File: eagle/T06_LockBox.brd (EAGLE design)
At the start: 100 x 80 mm, 28 parts, among them T1 2N3904, T2 2N3904, T3 2N3904

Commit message: small changes
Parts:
- moved R7 92.9 mm to (55.4, 8.38), turned to 180 degrees
- moved R6 92.1 mm to (55.4, 10.7), turned to 180 degrees
- moved R10 88.3 mm to (38.6, 10.7), turned to 90 degrees
- moved R3 85.8 mm to (47.2, 20.6)
- moved T3 83.8 mm to (53.3, 20.8)
- moved R9 83.0 mm to (35.3, 10.4), turned to 90 degrees
- moved R2 83.0 mm to (47.5, 18.2), turned to 180 degrees
- moved R4 81.6 mm to (84.3, 2.79)
- moved D1 79.2 mm to (91.4, 15.5), turned to 270 degrees
- moved R8 78.4 mm to (32.5, 10.7), turned to 90 degrees
- moved U$2 75.7 mm to (84.5, 58.4)
- moved JP1 75.3 mm to (90.3, 2.79)
- moved T2 74.1 mm to (53.5, 15.0)
- moved C5 67.9 mm to (89.3, 68.7), turned to 180 degrees
- moved R5 67.0 mm to (21.3, 20.3)
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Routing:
- net A0: track 69.3 -> 0.00 mm
- net A1: track 66.0 -> 0.00 mm
- net A2: track 55.2 -> 0.00 mm
- net START: track 20.0 -> 0.00 mm
- net 3.3V: track 3.52 -> 0.00 mm

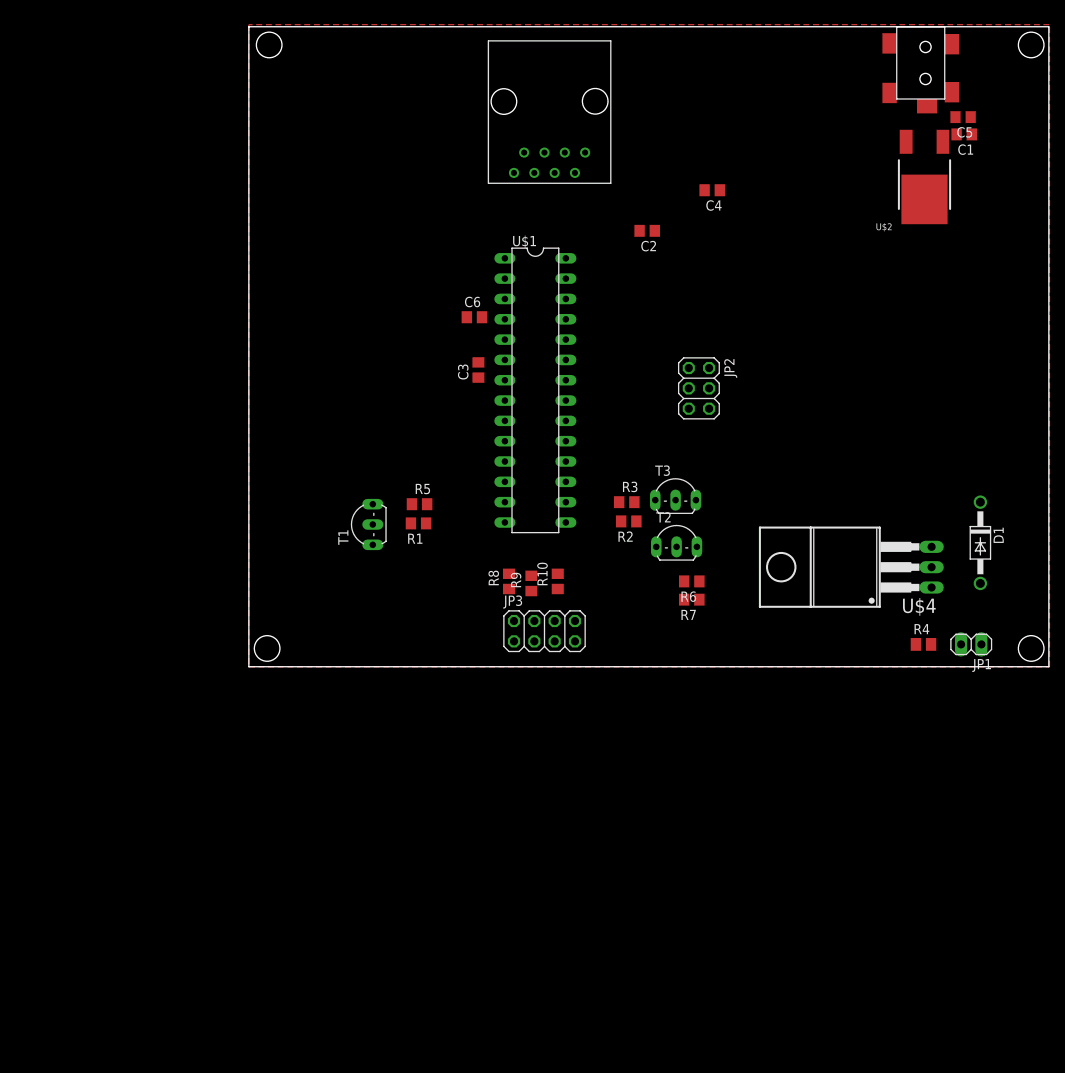
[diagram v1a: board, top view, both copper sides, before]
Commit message: Added connections to unused pins on the schematic.  Finished routing wires to the unused pin header locaton on the board.
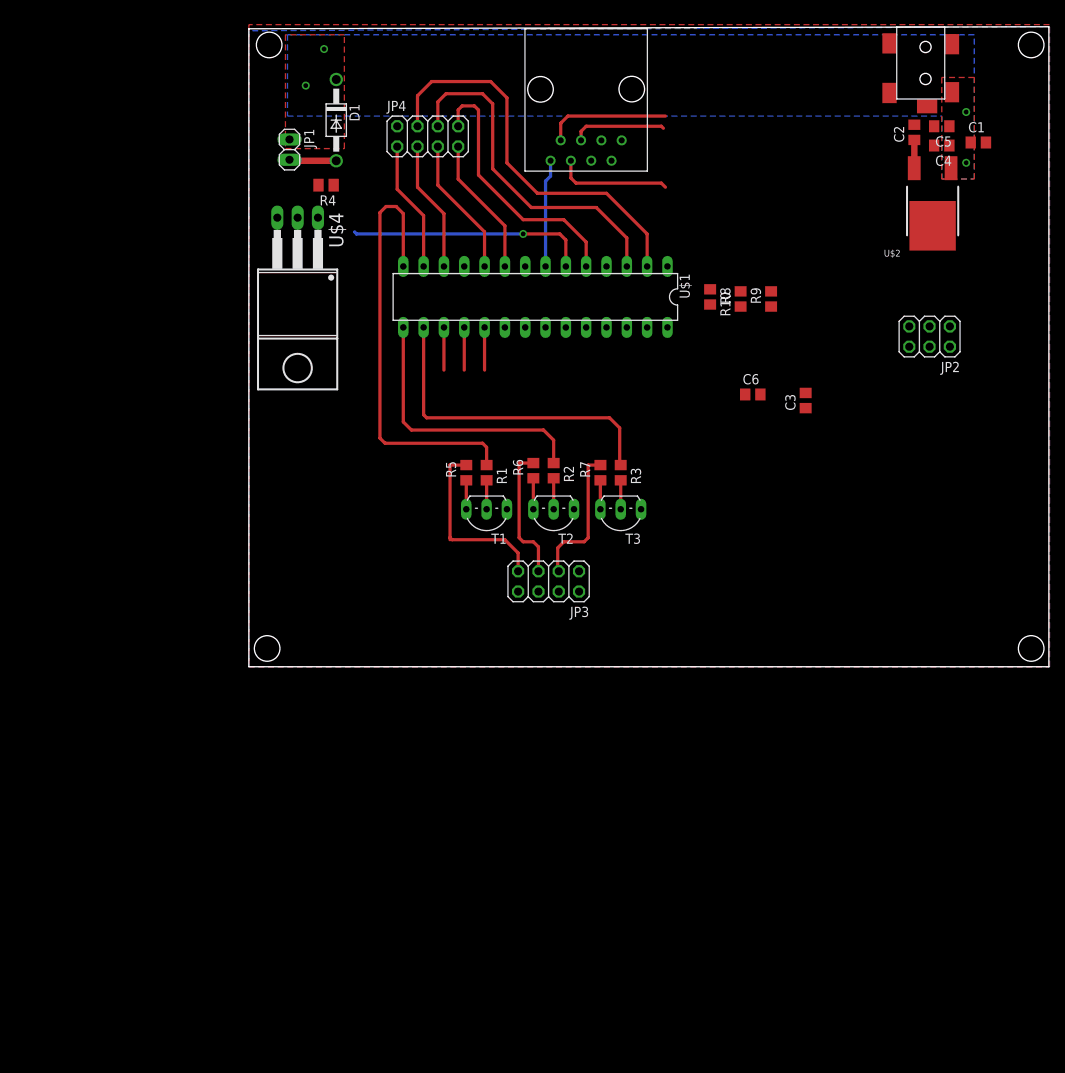
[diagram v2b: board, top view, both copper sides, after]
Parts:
- added JP4: UNUSED, T06_Lockbox:2X04
- C1, C2, C3, C4, C5, C6: device LockBox:C0805 -> T06_Lockbox:C0805
- D1: device LockBox:DO41-10 -> T06_Lockbox:DO41-10
- JP1: device LockBox:1X02 -> T06_Lockbox:1X02
- JP2: device LockBox:2X03 -> T06_Lockbox:2X03
- JP3: device LockBox:2X04 -> T06_Lockbox:2X04
- R1, R10, R2, R3, R5, R6, R7, R8, R9: device LockBox:R0805 -> T06_Lockbox:R0805
- R4: device LockBox:M0805 -> T06_Lockbox:M0805
- T1, T2, T3: device LockBox:TO92-BCE -> T06_Lockbox:TO92-BCE
- U$1: device LockBox:DIL28-3 -> T06_Lockbox:DIL28-3
- U$2: device LockBox:DPAK -> T06_Lockbox:DPAK
- U$3: device LockBox:PWR_JACK -> T06_Lockbox:PWR_JACK
- U$4: device LockBox:T0220-3 -> T06_Lockbox:T0220-3
- U$6: device LockBox:MODJACK8 -> T06_Lockbox:MODJACK8
- moved JP1 105.3 mm to (5.08, 64.6), turned to 270 degrees
- moved D1 96.3 mm to (10.9, 68.3)
- moved R4 94.2 mm to (9.65, 60.2), turned to 180 degrees
- moved U$4 75.1 mm to (6.10, 44.7), turned to 180 degrees
- moved R9 46.5 mm to (65.3, 46.0)
- moved R8 45.7 mm to (61.5, 46.0)
- moved C3 41.1 mm to (69.6, 33.3)
- moved R10 40.3 mm to (57.7, 46.2), turned to 270 degrees
- moved C6 36.1 mm to (63.0, 34.0)
- moved C2 35.6 mm to (83.2, 66.8), turned to 90 degrees
- moved JP2 29.5 mm to (85.1, 41.3), turned to 180 degrees
- moved C4 29.2 mm to (86.6, 65.2)
- moved R6 24.2 mm to (35.6, 24.5), turned to 90 degrees
- moved R7 19.6 mm to (43.9, 24.3), turned to 90 degrees
- moved T2 16.1 mm to (38.1, 19.7), turned to 180 degrees
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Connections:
- new net PB6: JP4.7, U$1.9
- new net PB7: JP4.5, U$1.10
- new net PD0: JP4.4, U$1.2
- new net PD1: JP4.6, U$1.3
- new net PD3: JP4.8, U$1.5
- new net PD6: JP4.3, U$1.12
- new net PD7: JP4.1, U$1.13
- net AREF: now also JP4.2
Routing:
- net RED: track 0.00 -> 54.4 mm
- net PD0: track 0.00 -> 50.0 mm
- net PD1: track 0.00 -> 42.9 mm
- net BLUE: track 0.00 -> 40.8 mm
- net GREEN: track 0.00 -> 34.4 mm
- net PD3: track 0.00 -> 33.1 mm
- net SOL_EN: track 0.00 -> 30.1 mm, vias 0 -> 1
- net EN_RD: track 0.00 -> 23.0 mm
- net EN_BL: track 0.00 -> 17.9 mm
- net PB7: track 0.00 -> 17.4 mm
- net PB6: track 0.00 -> 17.4 mm
- net EN_GR: track 0.00 -> 17.0 mm
- net 3.3V: track 0.00 -> 17.0 mm
- net PD7: track 0.00 -> 16.4 mm
- net PD6: track 0.00 -> 16.4 mm
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- added copper zone on layer 1, net +12V
- added copper zone on layer 16, net +12V
- added copper zone on layer 16, net N$2
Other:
- outline, holes or cut-outs redrawn

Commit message: Small changes
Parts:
- moved JP2 22.1 mm to (66.7, 53.5), turned to 90 degrees
- moved R10 0.13 mm to (57.7, 46.1), turned to 90 degrees
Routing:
- net LCD_RST: track 0.00 -> 29.6 mm
- net AREF: track 0.00 -> 23.1 mm, vias 0 -> 1
- net START: track 0.00 -> 14.0 mm
- net 3.3V: track 17.0 -> 28.2 mm
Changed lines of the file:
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@@
 <setting verticaltext="up"/>
 </settings>
-<grid distance="0.01" unitdist="inch" unit="inch" style="lines" multiple="1" display="yes" altdistance="0.01" altunitdist="inch" altunit="inch"/>
+<grid distance="0.005" unitdist="inch" unit="inch" style="lines" multiple="1" display="yes" altdistance="0.01" altunitdist="inch" altunit="inch"/>
 <layers>
 <layer number="1" name="Top" color="4" fill="1" visible="yes" active="yes"/>
@@
 <element name="D1" library="T06_Lockbox" package="DO41-10" value="1N4004" x="10.922" y="68.326" rot="R270"/>
 <element name="JP1" library="T06_Lockbox" package="1X02" value="Sol_ctrl" x="5.08" y="64.643" rot="R270"/>
-<element name="JP2" library="T06_Lockbox" package="2X03" value="ICSP" x="85.09" y="41.275" rot="R180"/>
+<element name="JP2" library="T06_Lockbox" package="2X03" value="ICSP" x="66.675" y="53.467" rot="R90"/>
 <element name="R4" library="T06_Lockbox" package="M0805" value="1k" x="9.652" y="60.198" rot="R180"/>
 <element name="U$1" library="T06_Lockbox" package="DIL28-3" value="ATMEGA328" x="35.814" y="46.228" rot="R180">
@@
 <element name="R8" library="T06_Lockbox" package="R0805" value="10k" x="61.468" y="45.974" rot="R90"/>
 <element name="R9" library="T06_Lockbox" package="R0805" value="4.7k" x="65.278" y="45.974" rot="R90"/>
-<element name="R10" library="T06_Lockbox" package="R0805" value="4.7k" x="57.658" y="46.228" rot="R270"/>
+<element name="R10" library="T06_Lockbox" package="R0805" value="4.7k" x="57.658" y="46.101" rot="R90"/>
 <element name="C4" library="T06_Lockbox" package="C0805" value="10uF" x="86.614" y="65.151" rot="R180">
 <attribute name="SPICEMODEL" value="NONE" x="86.614" y="65.151" size="1.778" layer="27" rot="R180" display="off"/>
@@
 <contactref element="U$1" pad="27"/>
 <contactref element="R10" pad="1"/>
-<wire x1="49.784" y1="42.418" x2="57.658" y2="47.178" width="0" layer="19" extent="1-1"/>
+<wire x1="49.784" y1="42.418" x2="57.658" y2="45.151" width="0" layer="19" extent="1-1"/>
 <wire x1="36.195" y1="9.398" x2="49.784" y2="42.418" width="0" layer="19" extent="1-1"/>
 </signal>
@@
 <contactref element="U$1" pad="4"/>
 <contactref element="C6" pad="1"/>
-<wire x1="44.704" y1="50.038" x2="42.794" y2="63.256" width="0" layer="19" extent="1-1"/>
-<wire x1="47.244" y1="42.418" x2="44.704" y2="50.038" width="0" layer="19" extent="1-1"/>
-<wire x1="62.042" y1="34.036" x2="47.244" y2="42.418" width="0" layer="19" extent="1-1"/>
+<wire x1="44.704" y1="50.038" x2="44.704" y2="59.817" width="0.4064" layer="16"/>
+<wire x1="44.704" y1="59.817" x2="42.799" y2="61.722" width="0.4064" layer="16"/>
+<wire x1="42.799" y1="61.722" x2="42.799" y2="63.251" width="0.4064" layer="16"/>
+<wire x1="42.799" y1="63.251" x2="42.794" y2="63.256" width="0.4064" layer="16"/>
+<wire x1="47.244" y1="42.418" x2="62.042" y2="34.036" width="0" layer="19" extent="1-1"/>
+<wire x1="44.704" y1="50.038" x2="47.244" y2="42.418" width="0" layer="19" extent="1-1"/>
 </signal>
 <signal name="+12V">
@@
 <contactref element="JP3" pad="2"/>
 <contactref element="R8" pad="1"/>
-<wire x1="26.924" y1="50.038" x2="61.468" y2="45.024" width="0" layer="19" extent="1-1"/>
-<wire x1="41.275" y1="9.398" x2="61.468" y2="45.024" width="0" layer="19" extent="1-1"/>
+<wire x1="26.924" y1="50.038" x2="26.924" y2="48.387" width="0.4064" layer="1"/>
+<wire x1="26.924" y1="48.387" x2="28.067" y2="47.244" width="0.4064" layer="1"/>
+<wire x1="28.067" y1="47.244" x2="54.356" y2="47.244" width="0.4064" layer="1"/>
+<wire x1="54.356" y1="47.244" x2="61.468" y2="45.024" width="0" layer="19" extent="1-1"/>
+<wire x1="41.275" y1="9.398" x2="54.356" y2="47.244" width="0" layer="19" extent="1-1"/>
 </signal>
 <signal name="SCL">
@@
 <contactref element="JP2" pad="4"/>
 <wire x1="24.384" y1="42.418" x2="24.384" y2="37.084" width="0.4064" layer="1"/>
-<wire x1="24.384" y1="42.418" x2="85.09" y2="40.005" width="0" layer="19" extent="1-1"/>
+<wire x1="24.384" y1="42.418" x2="65.405" y2="53.467" width="0" layer="19" extent="1-1"/>
 </signal>
 <signal name="SCK">
@@
 <contactref element="JP2" pad="3"/>
 <wire x1="29.464" y1="42.418" x2="29.464" y2="37.084" width="0.4064" layer="1"/>
-<wire x1="29.464" y1="42.418" x2="85.09" y2="42.545" width="0" layer="19" extent="1-1"/>
+<wire x1="29.464" y1="42.418" x2="67.945" y2="53.467" width="0" layer="19" extent="1-1"/>
 </signal>
 <signal name="!RST">
 <contactref element="U$1" pad="1"/>
 <contactref element="JP2" pad="5"/>
-<wire x1="52.324" y1="50.038" x2="82.55" y2="42.545" width="0" layer="19" extent="1-1"/>
+<wire x1="52.324" y1="50.038" x2="67.945" y2="56.007" width="0" layer="19" extent="1-1"/>
 </signal>
 <signal name="MISO">
@@
 <contactref element="JP2" pad="1"/>
 <wire x1="26.924" y1="42.418" x2="26.924" y2="37.084" width="0.4064" layer="1"/>
-<wire x1="26.924" y1="42.418" x2="87.63" y2="42.545" width="0" layer="19" extent="1-1"/>
+<wire x1="26.924" y1="42.418" x2="67.945" y2="50.927" width="0" layer="19" extent="1-1"/>
 </signal>
 <signal name="3.3V">
@@
 <wire x1="37.714" y1="61.336" x2="37.084" y2="60.706" width="0.4064" layer="16"/>
 <wire x1="37.084" y1="60.706" x2="37.084" y2="50.038" width="0.4064" layer="16"/>
-<wire x1="87.63" y1="40.005" x2="83.171" y2="62.318" width="0" layer="19" extent="1-1"/>
-<wire x1="69.596" y1="32.324" x2="87.63" y2="40.005" width="0" layer="19" extent="1-1"/>
-<wire x1="65.278" y1="46.924" x2="69.596" y2="32.324" width="0" layer="19" extent="1-1"/>
+<wire x1="37.084" y1="50.038" x2="37.084" y2="47.117" width="0.4064" layer="16"/>
+<wire x1="37.084" y1="47.117" x2="36.195" y2="46.228" width="0.4064" layer="16"/>
+<wire x1="36.195" y1="46.228" x2="33.782" y2="46.228" width="0.4064" layer="16"/>
+<wire x1="33.782" y1="46.228" x2="32.004" y2="44.45" width="0.4064" layer="16"/>
+<wire x1="32.004" y1="44.45" x2="32.004" y2="42.418" width="0.4064" layer="16"/>
+<wire x1="65.405" y1="50.927" x2="83.171" y2="62.318" width="0" layer="19" extent="1-1"/>
+<wire x1="65.278" y1="46.924" x2="65.405" y2="50.927" width="0" layer="19" extent="1-1"/>
 <wire x1="61.468" y1="46.924" x2="65.278" y2="46.924" width="0" layer="19" extent="1-1"/>
-<wire x1="57.658" y1="45.278" x2="61.468" y2="46.924" width="0" layer="19" extent="1-1"/>
-<wire x1="37.084" y1="50.038" x2="57.658" y2="45.278" width="0" layer="19" extent="1-1"/>
-<wire x1="32.004" y1="42.418" x2="37.084" y2="50.038" width="0" layer="19" extent="1-1"/>
+<wire x1="57.658" y1="47.051" x2="61.468" y2="46.924" width="0" layer="19" extent="1-1"/>
+<wire x1="69.596" y1="32.324" x2="65.278" y2="46.924" width="0" layer="19" extent="1-1"/>
+<wire x1="37.084" y1="47.117" x2="57.658" y2="47.051" width="0" layer="19" extent="1-16"/>
 <wire x1="41.275" y1="11.938" x2="32.004" y2="42.418" width="0" layer="19" extent="1-1"/>
 </signal>
@@
 <contactref element="U$1" pad="21"/>
 <contactref element="JP4" pad="2"/>
-<wire x1="34.544" y1="42.418" x2="18.542" y2="67.564" width="0" layer="19" extent="1-1"/>
+<wire x1="34.544" y1="42.418" x2="34.544" y2="44.196" width="0.4064" layer="1"/>
+<wire x1="34.544" y1="44.196" x2="33.401" y2="45.339" width="0.4064" layer="1"/>
+<wire x1="33.401" y1="45.339" x2="27.051" y2="45.339" width="0.4064" layer="1"/>
+<wire x1="27.051" y1="45.339" x2="26.162" y2="46.228" width="0.4064" layer="1"/>
+<via x="26.162" y="46.228" extent="1-16" drill="0.6"/>
+<wire x1="26.162" y1="46.228" x2="14.097" y2="46.228" width="0.4064" layer="16"/>
+<wire x1="14.097" y1="46.228" x2="18.542" y2="67.564" width="0" layer="19" extent="16-16"/>
 </signal>
 <signal name="PD7">

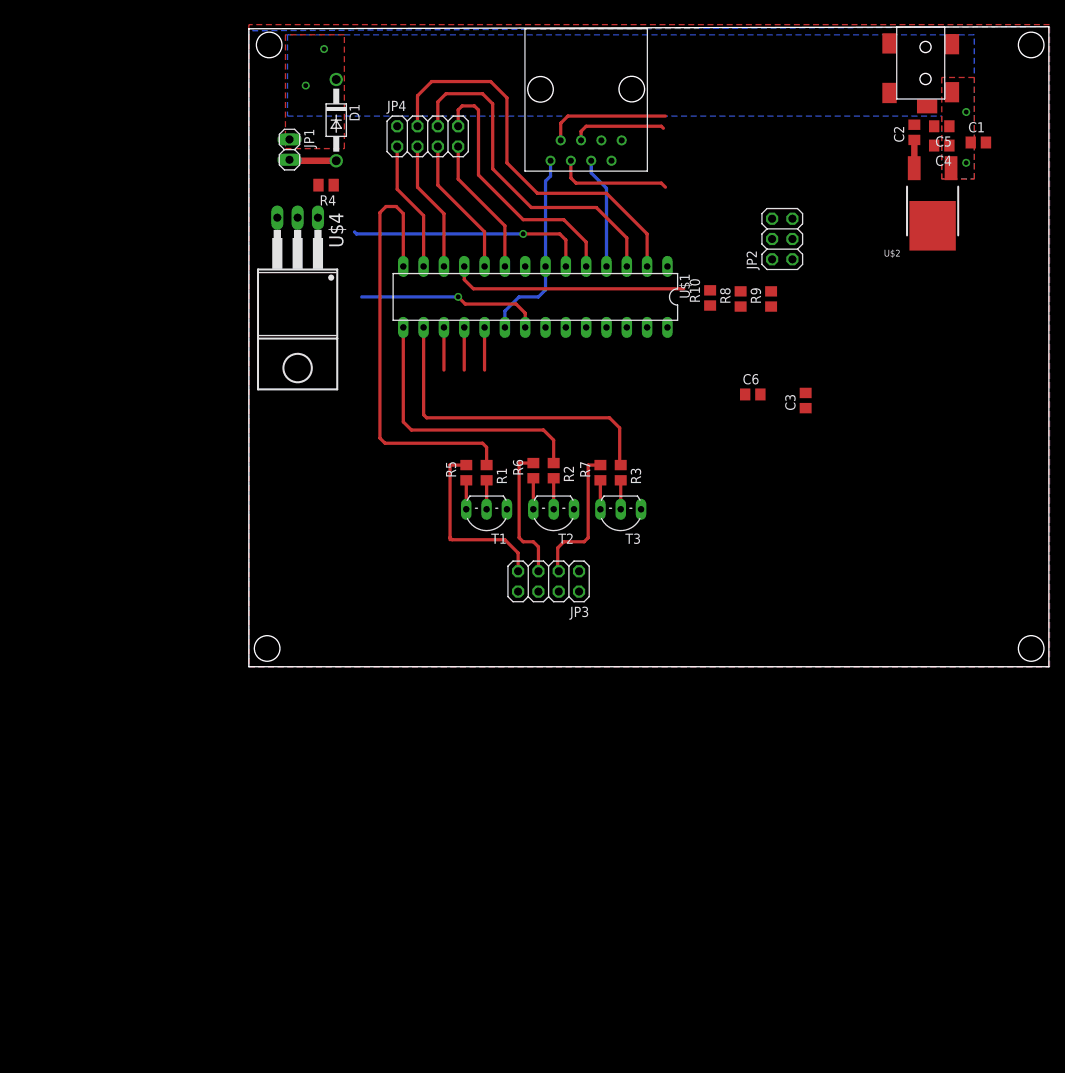
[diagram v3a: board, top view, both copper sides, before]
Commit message: Finished first REV of board layout.  Still need to add via's and update labeling for the t-slik layer.
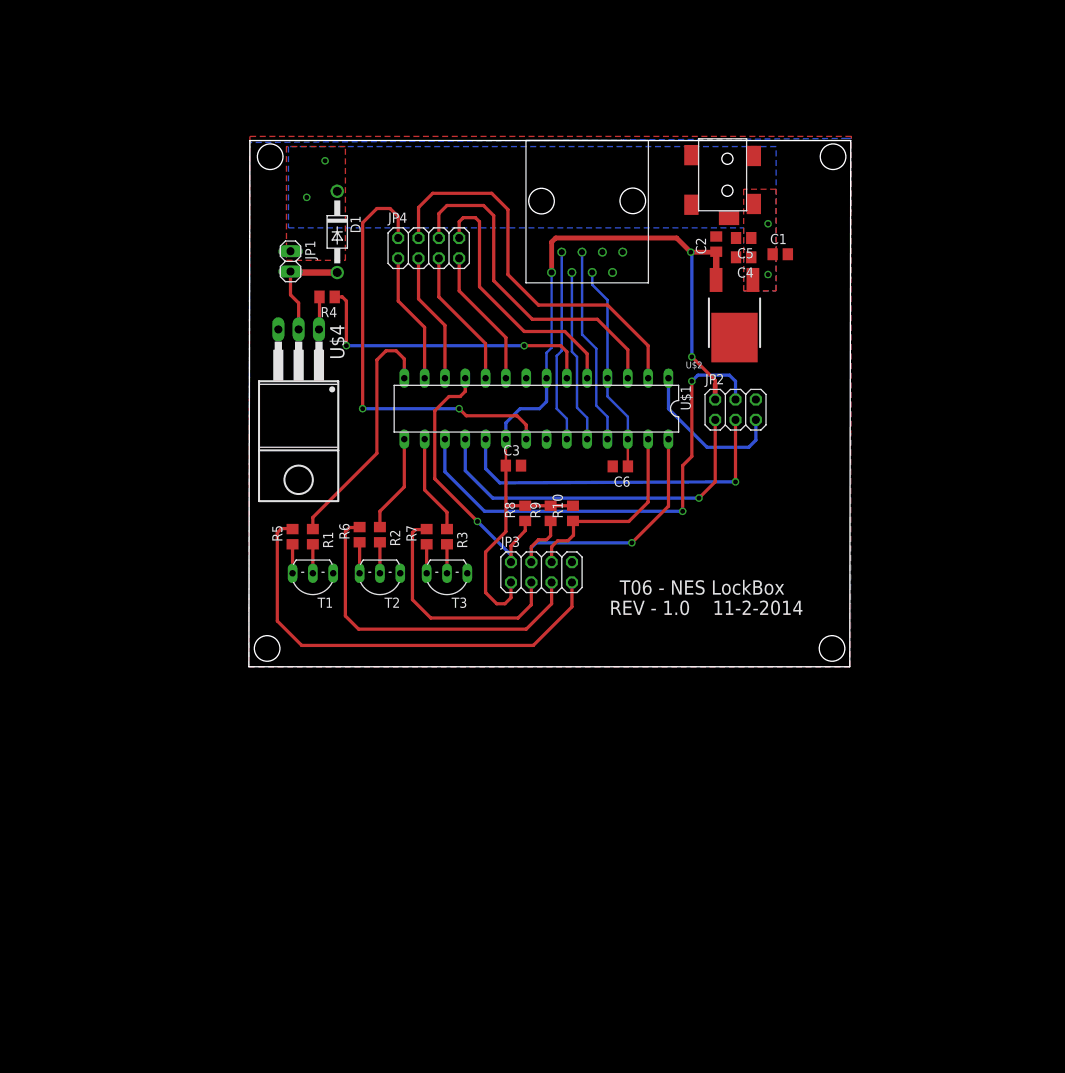
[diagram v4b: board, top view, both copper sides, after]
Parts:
- moved R9 38.4 mm to (37.7, 19.2)
- moved R8 38.0 mm to (34.5, 19.2)
- moved C3 37.4 mm to (33.1, 25.1), turned to 0 degrees
- moved R10 31.9 mm to (40.5, 19.2)
- moved C4 28.4 mm to (61.8, 51.2)
- moved C2 28.4 mm to (58.4, 52.8)
- moved C5 28.4 mm to (61.8, 53.6)
- moved C1 28.4 mm to (66.4, 51.6)
- moved U$2 28.4 mm to (60.7, 41.1)
- moved U$3 28.4 mm to (59.8, 63.5)
- moved T2 23.1 mm to (16.4, 11.7)
- moved R1 23.1 mm to (8.00, 16.3)
- moved R3 23.1 mm to (24.8, 16.3)
- moved R5 23.1 mm to (5.46, 16.3)
- moved R7 23.1 mm to (22.2, 16.3)
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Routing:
- net 3.3V: track 28.2 -> 107.8 mm, vias 0 -> 2
- net MOSI: track 5.33 -> 60.9 mm, vias 0 -> 2
- net MISO: track 5.33 -> 45.2 mm, vias 0 -> 1
- net SCK: track 5.33 -> 43.4 mm, vias 0 -> 1
- net SCL: track 0.00 -> 36.2 mm, vias 0 -> 1
- net EN_RD: track 23.0 -> 56.3 mm
- net AREF: track 23.1 -> 54.6 mm, vias 1 -> 2
- net BLUE: track 40.8 -> 12.4 mm
- net EN_GR: track 17.0 -> 43.0 mm
- net SDA: track 0.00 -> 25.3 mm
- net RED: track 54.4 -> 31.2 mm
- net GREEN: track 34.4 -> 12.3 mm
- net !RST: track 0.00 -> 19.6 mm
- net A2: track 11.8 -> 24.7 mm
- net START: track 14.0 -> 26.1 mm
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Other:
- board size 100 x 80 mm -> 75.2 x 65.8 mm
- board text added: "REV - 1.0 11-2-2014"
- board text added: "T06 - NES LockBox"
